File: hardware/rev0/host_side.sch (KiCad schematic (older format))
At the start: 9 parts, among them IC1 ECP5-BGA256, U11 USB3343

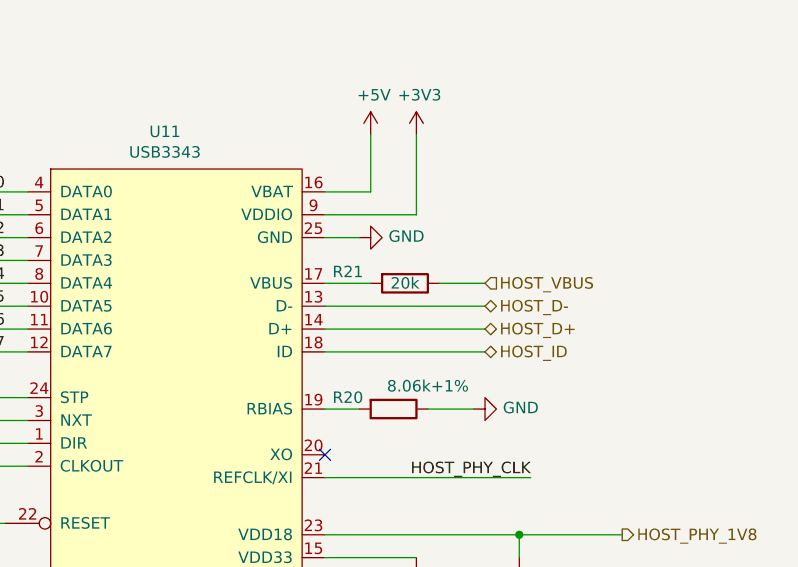
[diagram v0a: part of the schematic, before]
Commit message: hardware: add part numbers
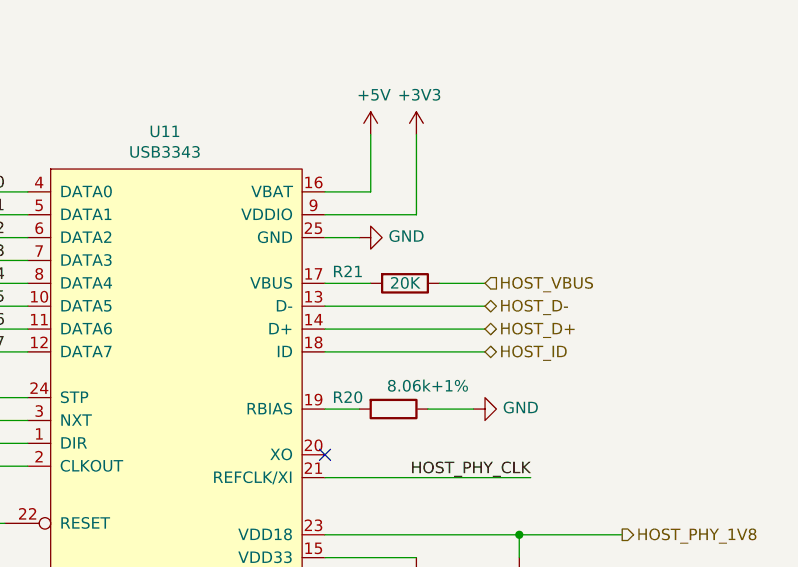
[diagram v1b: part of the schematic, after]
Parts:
- C48, C50: Manufacturer_Part_Number (none) -> GENERIC-CAP-0603-1uF
- R20: Description (none) -> RES SMD 8.06K OHM 1% 1/10W 0402; Manufacturer_Name (none) -> Panasonic; Manufacturer_Part_Number (none) -> ERJ-2RKF8061X
- R21: value 20k -> 20K; Description (none) -> RES 20K OHM 0.1% 1/16W 0402; Manufacturer_Name (none) -> TE Connectivity; Manufacturer_Part_Number (none) -> RP73PF1E20KBTDF
- R24: Manufacturer_Part_Number (none) -> GENERIC-RES-0402-10K
- U11: Description (none) -> IC TRANSCEIVER 1/1 24QFN; Manufacturer_Name (none) -> Microchip; Manufacturer_Part_Number (none) -> USB3343-CP
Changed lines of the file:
@@
 EESchema Schematic File Version 4
-LIBS:luna_rev0-cache
 EELAYER 30 0
 EELAYER END
@@
 Wire Wire Line
 	7000 2300 6800 2300
-$Comp
-L Device:R R?
-U 1 1 5DD9AF21
-P 7150 2300
-AR Path="/5DCD9772/5DD9AF21" Ref="R?"  Part="1"
-AR Path="/5DD754D4/5DD9AF21" Ref="R21"  Part="1"
-F 0 "R21" V 7100 2050 50  0000 C CNN
-F 1 "20k" V 7150 2300 50  0000 C CNN
-F 2 "Resistor_SMD:R_0402_1005Metric" V 7080 2300 50  0001 C CNN
-F 3 "~" H 7150 2300 50  0001 C CNN
-	1    7150 2300
-	0    1    1    0
-$EndComp
 Wire Wire Line
 	7450 2850 7250 2850
@@
 Wire Wire Line
 	6950 2850 6800 2850
-$Comp
-L Device:R R?
-U 1 1 5DD9AF13
-P 7100 2850
-AR Path="/5DCD9772/5DD9AF13" Ref="R?"  Part="1"
-AR Path="/5DD754D4/5DD9AF13" Ref="R20"  Part="1"
-F 0 "R20" V 7050 2650 50  0000 C CNN
-F 1 "8.06k+1%" V 7000 3000 50  0000 C CNN
-F 2 "Resistor_SMD:R_0402_1005Metric" V 7030 2850 50  0001 C CNN
-F 3 "~" H 7100 2850 50  0001 C CNN
-	1    7100 2850
-	0    1    1    0
-$EndComp
 Wire Wire Line
 	7200 2000 6800 2000
@@
 	1    0    0    -1
 $EndComp
-$Comp
-L Device:C C?
-U 1 1 5DD9AED1
-P 7650 3650
-AR Path="/5DCD9772/5DD9AED1" Ref="C?"  Part="1"
-AR Path="/5DD754D4/5DD9AED1" Ref="C50"  Part="1"
-F 0 "C50" H 7765 3695 50  0000 L CNN
-F 1 "1uF" H 7765 3605 50  0000 L CNN
-F 2 "Capacitor_SMD:C_0603_1608Metric" H 7688 3500 50  0001 C CNN
-F 3 "~" H 7650 3650 50  0001 C CNN
-	1    7650 3650
-	1    0    0    -1
-$EndComp
 Wire Wire Line
 	7200 3950 7200 3800
@@
 F 3 "" H 7200 3950 50  0001 C CNN
 	1    7200 3950
-	1    0    0    -1
-$EndComp
-$Comp
-L Device:C C?
-U 1 1 5DD9AEC3
-P 7200 3650
-AR Path="/5DCD9772/5DD9AEC3" Ref="C?"  Part="1"
-AR Path="/5DD754D4/5DD9AEC3" Ref="C48"  Part="1"
-F 0 "C48" H 7315 3695 50  0000 L CNN
-F 1 "1uF" H 7315 3605 50  0000 L CNN
-F 2 "Capacitor_SMD:C_0603_1608Metric" H 7238 3500 50  0001 C CNN
-F 3 "~" H 7200 3650 50  0001 C CNN
-	1    7200 3650
 	1    0    0    -1
 $EndComp
@@
 $EndComp
 $Comp
-L Device:C C?
-U 1 1 5DEDB896
-P 6750 5200
-AR Path="/5DCD9772/5DEDB896" Ref="C?"  Part="1"
-AR Path="/5DD754D4/5DEDB896" Ref="C47"  Part="1"
-F 0 "C47" H 6865 5245 50  0000 L CNN
-F 1 "0.1uF" H 6865 5155 50  0000 L CNN
-F 2 "Capacitor_SMD:C_0402_1005Metric" H 6788 5050 50  0001 C CNN
-F 3 "~" H 6750 5200 50  0001 C CNN
-	1    6750 5200
-	1    0    0    -1
-$EndComp
-$Comp
-L Device:C C?
-U 1 1 5DEDB89C
-P 7250 5200
-AR Path="/5DCD9772/5DEDB89C" Ref="C?"  Part="1"
-AR Path="/5DD754D4/5DEDB89C" Ref="C49"  Part="1"
-F 0 "C49" H 7365 5245 50  0000 L CNN
-F 1 "0.1uF" H 7365 5155 50  0000 L CNN
-F 2 "Capacitor_SMD:C_0402_1005Metric" H 7288 5050 50  0001 C CNN
-F 3 "~" H 7250 5200 50  0001 C CNN
-	1    7250 5200
-	1    0    0    -1
-$EndComp
-$Comp
 L power:+5V #PWR?
 U 1 1 5DEDB8A2
@@
 Wire Wire Line
 	7250 5350 7250 5450
-$Comp
-L Device:R R24
-U 1 1 5E14D51C
-P 5000 3350
-F 0 "R24" V 5100 3350 50  0000 C CNN
-F 1 "10K" V 5000 3350 50  0000 C CNN
-F 2 "Resistor_SMD:R_0402_1005Metric" V 4930 3350 50  0001 C CNN
-F 3 "~" H 5000 3350 50  0001 C CNN
-	1    5000 3350
-	0    1    1    0
-$EndComp
 Wire Wire Line
 	5150 3350 5250 3350
@@
 Entry Wire Line
 	4350 5450 4450 5550
-$Comp
-L usb:USB3343 U?
-U 1 1 5DD9AEA4
-P 5500 1800
-AR Path="/5DCD9772/5DD9AEA4" Ref="U?"  Part="1"
-AR Path="/5DD754D4/5DD9AEA4" Ref="U11"  Part="1"
-F 0 "U11" H 6100 1963 50  0000 C CNN
-F 1 "USB3343" H 6100 1873 50  0000 C CNN
-F 2 "Package_DFN_QFN:VQFN-24-1EP_4x4mm_P0.5mm_EP2.45x2.45mm" H 5500 1800 50  0001 C CNN
-F 3 "http://ww1.microchip.com/downloads/en/DeviceDoc/334x.pdf" H 5500 1800 50  0001 C CNN
-	1    5500 1800
-	1    0    0    -1
-$EndComp
 Wire Wire Line
 	5500 1900 4550 1900
@@
 Text Label 2850 1900 0    50   ~ 0
 HOST_DATA7
+Wire Wire Line
+	2700 4850 4350 4850
+Entry Wire Line
+	4350 4850 4450 4950
+Entry Wire Line
+	4350 4850 4450 4950
+Text Label 2850 4850 0    50   ~ 0
+HOST_NXT
+Wire Wire Line
+	7650 3400 8100 3400
+Wire Wire Line
+	6800 3500 7200 3500
+Wire Bus Line
+	4450 1650 4450 5800
+$Comp
+L Device:R R?
+U 1 1 5DD9AF21
+P 7150 2300
+AR Path="/5DCD9772/5DD9AF21" Ref="R?"  Part="1"
+AR Path="/5DD754D4/5DD9AF21" Ref="R21"  Part="1"
+F 0 "R21" V 7100 2050 50  0000 C CNN
+F 1 "20K" V 7150 2300 50  0000 C CNN
+F 2 "Resistor_SMD:R_0402_1005Metric" V 7080 2300 50  0001 C CNN
+F 3 "~" H 7150 2300 50  0001 C CNN
+F 4 "RES 20K OHM 0.1% 1/16W 0402" H 7150 2300 50  0001 C CNN "Description"
+F 5 "TE Connectivity" H 7150 2300 50  0001 C CNN "Manufacturer_Name"
+F 6 "RP73PF1E20KBTDF" H 7150 2300 50  0001 C CNN "Manufacturer_Part_Number"
+	1    7150 2300
+	0    1    1    0
+$EndComp
+$Comp
+L Device:R R?
+U 1 1 5DD9AF13
+P 7100 2850
+AR Path="/5DCD9772/5DD9AF13" Ref="R?"  Part="1"
+AR Path="/5DD754D4/5DD9AF13" Ref="R20"  Part="1"
+F 0 "R20" V 7050 2650 50  0000 C CNN
+F 1 "8.06k+1%" V 7000 3000 50  0000 C CNN
+F 2 "Resistor_SMD:R_0402_1005Metric" V 7030 2850 50  0001 C CNN
+F 3 "~" H 7100 2850 50  0001 C CNN
+F 4 "RES SMD 8.06K OHM 1% 1/10W 0402" H 7100 2850 50  0001 C CNN "Description"
+F 5 "Panasonic" H 7100 2850 50  0001 C CNN "Manufacturer_Name"
+F 6 "ERJ-2RKF8061X" H 7100 2850 50  0001 C CNN "Manufacturer_Part_Number"
+	1    7100 2850
+	0    1    1    0
+$EndComp
+$Comp
+L Device:C C?
+U 1 1 5DD9AED1
+P 7650 3650
+AR Path="/5DCD9772/5DD9AED1" Ref="C?"  Part="1"
+AR Path="/5DD754D4/5DD9AED1" Ref="C50"  Part="1"
+F 0 "C50" H 7765 3695 50  0000 L CNN
+F 1 "1uF" H 7765 3605 50  0000 L CNN
+F 2 "Capacitor_SMD:C_0603_1608Metric" H 7688 3500 50  0001 C CNN
+F 3 "~" H 7650 3650 50  0001 C CNN
+F 4 "GENERIC-CAP-0603-1uF" H 7650 3650 50  0001 C CNN "Manufacturer_Part_Number"
+	1    7650 3650
+	1    0    0    -1
+$EndComp
+$Comp
+L Device:C C?
+U 1 1 5DD9AEC3
+P 7200 3650
+AR Path="/5DCD9772/5DD9AEC3" Ref="C?"  Part="1"
+AR Path="/5DD754D4/5DD9AEC3" Ref="C48"  Part="1"
+F 0 "C48" H 7315 3695 50  0000 L CNN
+F 1 "1uF" H 7315 3605 50  0000 L CNN
+F 2 "Capacitor_SMD:C_0603_1608Metric" H 7238 3500 50  0001 C CNN
+F 3 "~" H 7200 3650 50  0001 C CNN
+F 4 "GENERIC-CAP-0603-1uF" H 7200 3650 50  0001 C CNN "Manufacturer_Part_Number"
+	1    7200 3650
+	1    0    0    -1
+$EndComp
+$Comp
+L Device:C C?
+U 1 1 5DEDB896
+P 6750 5200
+AR Path="/5DCD9772/5DEDB896" Ref="C?"  Part="1"
+AR Path="/5DD754D4/5DEDB896" Ref="C47"  Part="1"
+F 0 "C47" H 6865 5245 50  0000 L CNN
+F 1 "0.1uF" H 6865 5155 50  0000 L CNN
+F 2 "Capacitor_SMD:C_0402_1005Metric" H 6788 5050 50  0001 C CNN
+F 3 "~" H 6750 5200 50  0001 C CNN
+	1    6750 5200
+	1    0    0    -1
+$EndComp
+$Comp
+L Device:C C?
+U 1 1 5DEDB89C
+P 7250 5200
+AR Path="/5DCD9772/5DEDB89C" Ref="C?"  Part="1"
+AR Path="/5DD754D4/5DEDB89C" Ref="C49"  Part="1"
+F 0 "C49" H 7365 5245 50  0000 L CNN
+F 1 "0.1uF" H 7365 5155 50  0000 L CNN
+F 2 "Capacitor_SMD:C_0402_1005Metric" H 7288 5050 50  0001 C CNN
+F 3 "~" H 7250 5200 50  0001 C CNN
+	1    7250 5200
+	1    0    0    -1
+$EndComp
+$Comp
+L Device:R R24
+U 1 1 5E14D51C
+P 5000 3350
+F 0 "R24" V 5100 3350 50  0000 C CNN
+F 1 "10K" V 5000 3350 50  0000 C CNN
+F 2 "Resistor_SMD:R_0402_1005Metric" V 4930 3350 50  0001 C CNN
+F 3 "~" H 5000 3350 50  0001 C CNN
+F 4 "GENERIC-RES-0402-10K" H 5000 3350 50  0001 C CNN "Manufacturer_Part_Number"
+	1    5000 3350
+	0    1    1    0
+$EndComp
+$Comp
+L usb:USB3343 U?
+U 1 1 5DD9AEA4
+P 5500 1800
+AR Path="/5DCD9772/5DD9AEA4" Ref="U?"  Part="1"
+AR Path="/5DD754D4/5DD9AEA4" Ref="U11"  Part="1"
+F 0 "U11" H 6100 1963 50  0000 C CNN
+F 1 "USB3343" H 6100 1873 50  0000 C CNN
+F 2 "Package_DFN_QFN:VQFN-24-1EP_4x4mm_P0.5mm_EP2.45x2.45mm" H 5500 1800 50  0001 C CNN
+F 3 "http://ww1.microchip.com/downloads/en/DeviceDoc/334x.pdf" H 5500 1800 50  0001 C CNN
+F 4 "IC TRANSCEIVER 1/1 24QFN" H 5500 1800 50  0001 C CNN "Description"
+F 5 "Microchip" H 5500 1800 50  0001 C CNN "Manufacturer_Name"
+F 6 "USB3343-CP" H 5500 1800 50  0001 C CNN "Manufacturer_Part_Number"
+	1    5500 1800
+	1    0    0    -1
+$EndComp
 $Comp
 L fpgas_and_processors:ECP5-BGA256 IC1
@@
 	1    0    0    -1
 $EndComp
-Wire Wire Line
-	2700 4850 4350 4850
-Entry Wire Line
-	4350 4850 4450 4950
-Entry Wire Line
-	4350 4850 4450 4950
-Text Label 2850 4850 0    50   ~ 0
-HOST_NXT
-Wire Wire Line
-	7650 3400 8100 3400
-Wire Wire Line
-	6800 3500 7200 3500
-Wire Bus Line
-	4450 1650 4450 5800
 $EndSCHEMATC

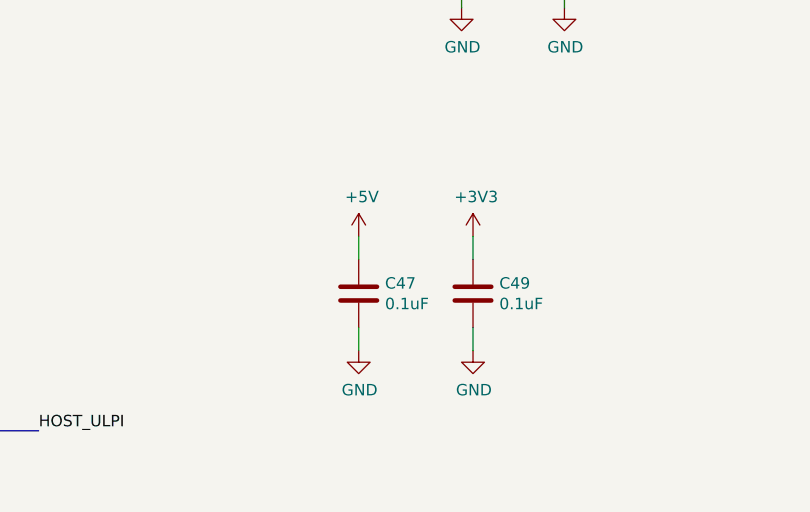
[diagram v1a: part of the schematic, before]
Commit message: hardware: update capacitors in schematic
Add parts that were in layout but were missing from schematic.
Update schematic to better represent r0.2 as manufactured.
fix #10
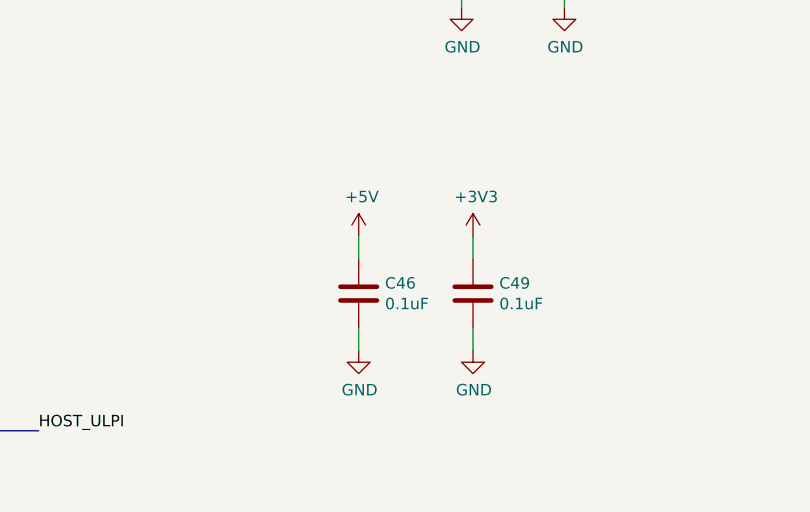
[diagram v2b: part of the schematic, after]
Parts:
- renumbered C47 to C46
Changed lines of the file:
@@
 Wire Wire Line
 	6800 3500 7200 3500
-Wire Bus Line
-	4450 1650 4450 5800
 $Comp
 L Device:R R?
@@
 $Comp
 L Device:C C?
-U 1 1 5DEDB896
-P 6750 5200
-AR Path="/5DCD9772/5DEDB896" Ref="C?"  Part="1"
-AR Path="/5DD754D4/5DEDB896" Ref="C47"  Part="1"
-F 0 "C47" H 6865 5245 50  0000 L CNN
-F 1 "0.1uF" H 6865 5155 50  0000 L CNN
-F 2 "Capacitor_SMD:C_0402_1005Metric" H 6788 5050 50  0001 C CNN
-F 3 "~" H 6750 5200 50  0001 C CNN
-	1    6750 5200
-	1    0    0    -1
-$EndComp
-$Comp
-L Device:C C?
 U 1 1 5DEDB89C
 P 7250 5200
@@
 	1    0    0    -1
 $EndComp
+Wire Bus Line
+	4450 1650 4450 5800
+$Comp
+L Device:C C?
+U 1 1 5DEDB896
+P 6750 5200
+AR Path="/5DCD9772/5DEDB896" Ref="C?"  Part="1"
+AR Path="/5DD754D4/5DEDB896" Ref="C46"  Part="1"
+F 0 "C46" H 6865 5245 50  0000 L CNN
+F 1 "0.1uF" H 6865 5155 50  0000 L CNN
+F 2 "Capacitor_SMD:C_0402_1005Metric" H 6788 5050 50  0001 C CNN
+F 3 "~" H 6750 5200 50  0001 C CNN
+	1    6750 5200
+	1    0    0    -1
+$EndComp

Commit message: hardware: normalize BOM fields
make compatible with kicad-bom-scripts
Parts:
- C46, C49: Part Number (none) -> GENERIC-CAP-0402-0.1uF
- C48, C50: Manufacturer_Part_Number GENERIC-CAP-0603-1uF -> (none); Part Number (none) -> GENERIC-CAP-0603-1uF
- IC1: Height 1.7 -> (none); Manufacturer (none) -> Lattice; Manufacturer_Name Lattice -> (none); Manufacturer_Part_Number LFE5U-12F-6BG256C -> (none); Mouser Part Number 842-LFE5U12F6BG256C -> (none); Mouser Price/Stock https://www.mouser.com/Search/Refine.aspx?Keyword=842-LFE5U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 -> (none); Part Number (none) -> LFE5U-12F-6BG256C
- R20: Manufacturer (none) -> Panasonic; Manufacturer_Name Panasonic -> (none); Manufacturer_Part_Number ERJ-2RKF8061X -> (none); Part Number (none) -> ERJ-2RKF8061X
- R21: Manufacturer (none) -> TE Connectivity; Manufacturer_Name TE Connectivity -> (none); Manufacturer_Part_Number RP73PF1E20KBTDF -> (none); Part Number (none) -> RP73PF1E20KBTDF
- R24: Manufacturer_Part_Number GENERIC-RES-0402-10K -> (none); Part Number (none) -> GENERIC-RES-0402-10K
- U11: Manufacturer (none) -> Microchip; Manufacturer_Name Microchip -> (none); Manufacturer_Part_Number USB3343-CP -> (none); Part Number (none) -> USB3343-CP
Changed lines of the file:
@@
 F 3 "~" H 7150 2300 50  0001 C CNN
 F 4 "RES 20K OHM 0.1% 1/16W 0402" H 7150 2300 50  0001 C CNN "Description"
-F 5 "TE Connectivity" H 7150 2300 50  0001 C CNN "Manufacturer_Name"
-F 6 "RP73PF1E20KBTDF" H 7150 2300 50  0001 C CNN "Manufacturer_Part_Number"
+F 5 "TE Connectivity" H 7150 2300 50  0001 C CNN "Manufacturer"
+F 6 "RP73PF1E20KBTDF" H 7150 2300 50  0001 C CNN "Part Number"
 	1    7150 2300
 	0    1    1    0
@@
 F 3 "~" H 7100 2850 50  0001 C CNN
 F 4 "RES SMD 8.06K OHM 1% 1/10W 0402" H 7100 2850 50  0001 C CNN "Description"
-F 5 "Panasonic" H 7100 2850 50  0001 C CNN "Manufacturer_Name"
-F 6 "ERJ-2RKF8061X" H 7100 2850 50  0001 C CNN "Manufacturer_Part_Number"
+F 5 "Panasonic" H 7100 2850 50  0001 C CNN "Manufacturer"
+F 6 "ERJ-2RKF8061X" H 7100 2850 50  0001 C CNN "Part Number"
 	1    7100 2850
 	0    1    1    0
@@
 F 2 "Capacitor_SMD:C_0603_1608Metric" H 7688 3500 50  0001 C CNN
 F 3 "~" H 7650 3650 50  0001 C CNN
-F 4 "GENERIC-CAP-0603-1uF" H 7650 3650 50  0001 C CNN "Manufacturer_Part_Number"
+F 4 "GENERIC-CAP-0603-1uF" H 7650 3650 50  0001 C CNN "Part Number"
 	1    7650 3650
 	1    0    0    -1
@@
 F 2 "Capacitor_SMD:C_0603_1608Metric" H 7238 3500 50  0001 C CNN
 F 3 "~" H 7200 3650 50  0001 C CNN
-F 4 "GENERIC-CAP-0603-1uF" H 7200 3650 50  0001 C CNN "Manufacturer_Part_Number"
+F 4 "GENERIC-CAP-0603-1uF" H 7200 3650 50  0001 C CNN "Part Number"
 	1    7200 3650
 	1    0    0    -1
@@
 F 2 "Capacitor_SMD:C_0402_1005Metric" H 7288 5050 50  0001 C CNN
 F 3 "~" H 7250 5200 50  0001 C CNN
+F 4 "GENERIC-CAP-0402-0.1uF" H 7250 5200 50  0001 C CNN "Part Number"
 	1    7250 5200
 	1    0    0    -1
@@
 F 2 "Resistor_SMD:R_0402_1005Metric" V 4930 3350 50  0001 C CNN
 F 3 "~" H 5000 3350 50  0001 C CNN
-F 4 "GENERIC-RES-0402-10K" H 5000 3350 50  0001 C CNN "Manufacturer_Part_Number"
+F 4 "GENERIC-RES-0402-10K" H 5000 3350 50  0001 C CNN "Part Number"
 	1    5000 3350
 	0    1    1    0
@@
 F 3 "http://ww1.microchip.com/downloads/en/DeviceDoc/334x.pdf" H 5500 1800 50  0001 C CNN
 F 4 "IC TRANSCEIVER 1/1 24QFN" H 5500 1800 50  0001 C CNN "Description"
-F 5 "Microchip" H 5500 1800 50  0001 C CNN "Manufacturer_Name"
-F 6 "USB3343-CP" H 5500 1800 50  0001 C CNN "Manufacturer_Part_Number"
+F 5 "Microchip" H 5500 1800 50  0001 C CNN "Manufacturer"
+F 6 "USB3343-CP" H 5500 1800 50  0001 C CNN "Part Number"
 	1    5500 1800
 	1    0    0    -1
@@
 F 3 "" H -1950 5900 50  0001 L CNN
 F 4 "FPGA - Field Programmable Gate Array ECP5; 12k LUTs; 1.1V" H -1950 5800 50  0001 L CNN "Description"
-F 5 "1.7" H -1950 6150 50  0001 L CNN "Height"
-F 6 "Lattice" H -1900 6750 50  0001 L CNN "Manufacturer_Name"
-F 7 "LFE5U-12F-6BG256C" H -1900 6650 50  0001 L CNN "Manufacturer_Part_Number"
-F 8 "842-LFE5U12F6BG256C" H -1250 5350 50  0001 L CNN "Mouser Part Number"
-F 9 "https://www.mouser.com/Search/Refine.aspx?Keyword=842-LFE5U12F6BG256C" H -1600 5200 50  0001 L CNN "Mouser Price/Stock"
+F 5 "Lattice" H -1900 6750 50  0001 L CNN "Manufacturer"
+F 6 "LFE5U-12F-6BG256C" H -1900 6650 50  0001 L CNN "Part Number"
 	7    1700 1500
 	1    0    0    -1
@@
 F 2 "Capacitor_SMD:C_0402_1005Metric" H 6788 5050 50  0001 C CNN
 F 3 "~" H 6750 5200 50  0001 C CNN
+F 4 "GENERIC-CAP-0402-0.1uF" H 6750 5200 50  0001 C CNN "Part Number"
 	1    6750 5200
 	1    0    0    -1
